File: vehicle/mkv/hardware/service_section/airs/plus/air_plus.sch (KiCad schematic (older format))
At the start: 11 parts, among them J1 UF_4_VT, J2 MicroFit_RA_06, J3 MicroFit_RA_4, J4 redcude_7461166, J5 redcude_7461166, K1 3350-4275-126(NC)

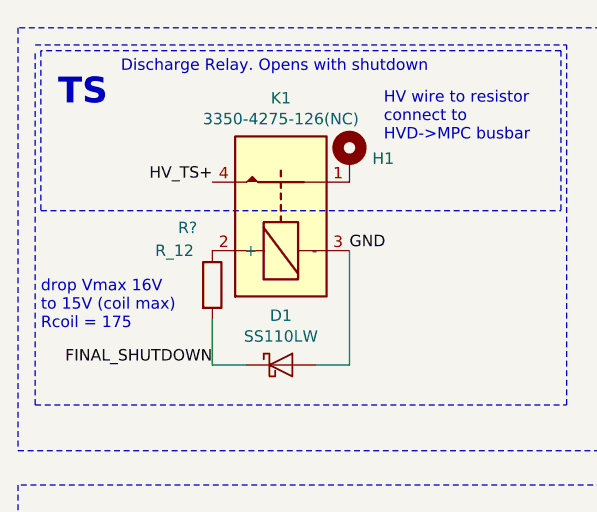
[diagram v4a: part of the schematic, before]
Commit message: fix: add resistor to limit relay voltage to operating range
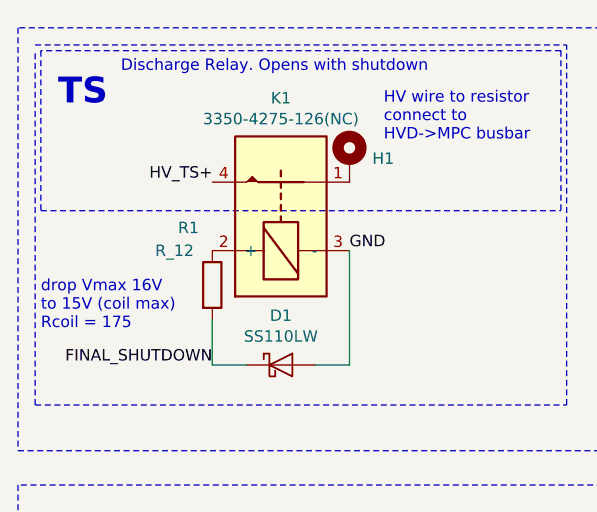
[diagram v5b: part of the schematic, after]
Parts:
- gave numbers to parts that had none: 1
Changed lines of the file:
@@
 drop Vmax 16V \nto 15V (coil max)\nRcoil = 175
 $Comp
-L formula:R_12 R?
+L formula:R_12 R1
 U 1 1 6262A6E0
 P 1600 1950
-F 0 "R?" H 1450 2200 50  0000 L CNN
+F 0 "R1" H 1450 2200 50  0000 L CNN
 F 1 "R_12" H 1350 2100 50  0000 L CNN
 F 2 "footprints:R_0805_OEM" V 1530 1950 50  0001 C CNN

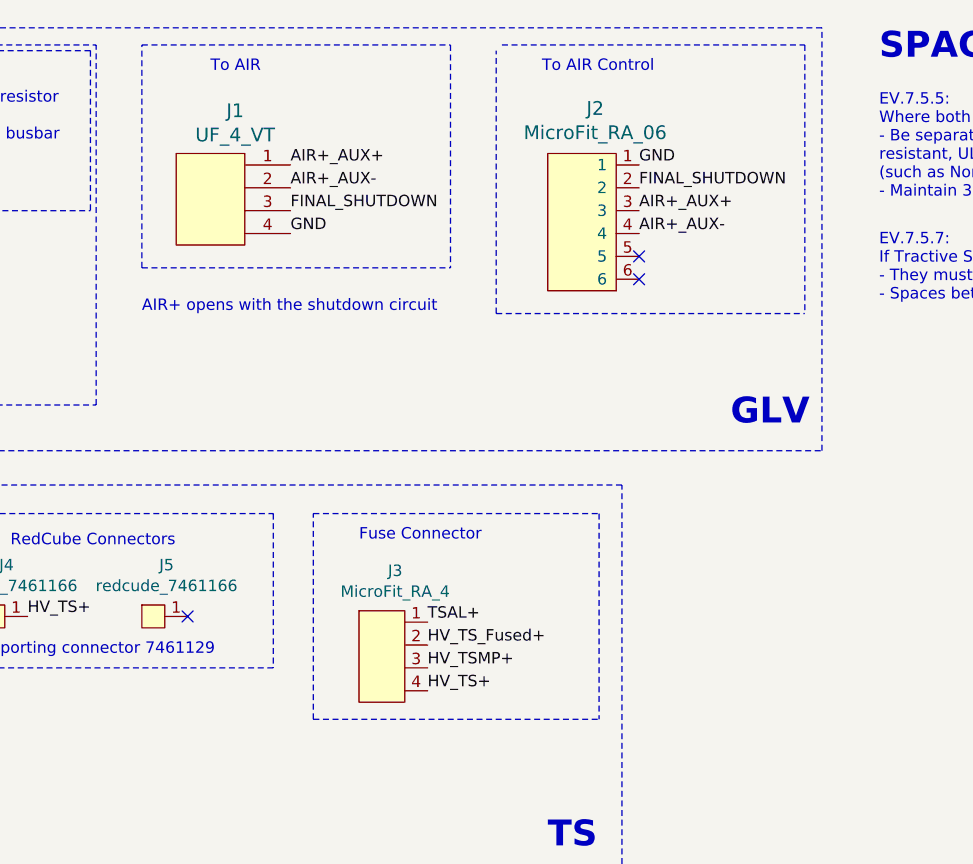
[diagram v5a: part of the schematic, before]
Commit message: feat: switch to microfit vt 4 where possible
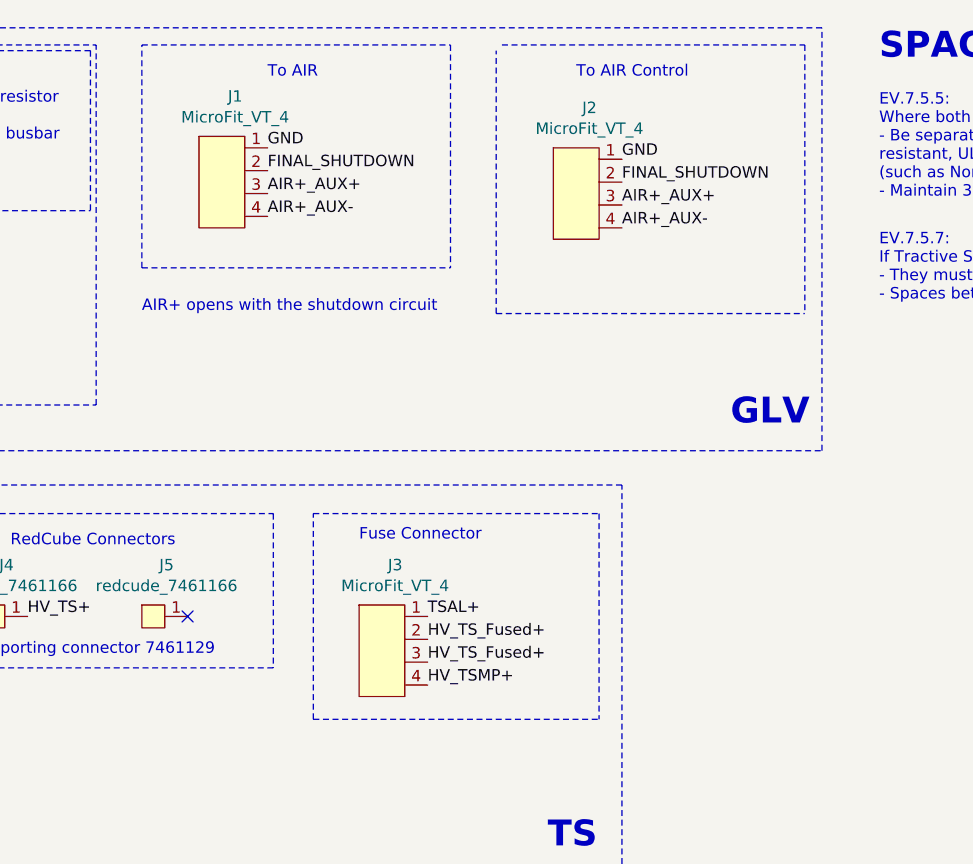
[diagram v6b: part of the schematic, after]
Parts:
- removed J1: UF_4_VT, footprints:Ultrafit_4, symbol Formula:UF_4_VT
- removed J2: MicroFit_RA_06, footprints:MicroFit_RA_06, symbol Formula:MicroFit_RA_06
- removed J3: MicroFit_RA_4, footprints:MicroFit_RA_4, symbol Formula:MicroFit_RA_4
- added J1, J2, J3: MicroFit_VT_4, footprints:MicroFit_VT_4, symbol formula:MicroFit_VT_4
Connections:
- net AIR+_AUX+: now also J1.3, J2.3
- net AIR+_AUX-: now also J1.4, J2.4
- net FINAL_SHUTDOWN: now also J1.2, J2.2
- net GND: now also J1.1, J2.1
- net HV_TSMP+: now also J3.4
- net HV_TS_Fused+: now also J3.1, J3.2, J3.3
- no-connect marks 3 -> 1
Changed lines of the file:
@@
 HV_TS+
-$Comp
-L Formula:UF_4_VT J1
-U 1 1 5DB02E97
-P 3650 1625
-F 0 "J1" H 3758 2062 60  0000 C CNN
-F 1 "UF_4_VT" H 3758 1956 60  0000 C CNN
-F 2 "footprints:Ultrafit_4" H 3550 1875 60  0001 C CNN
-F 3 "http://www.literature.molex.com/SQLImages/kelmscott/Molex/PDF_Images/987651-1008.pdf" H 3650 1975 60  0001 C CNN
-F 4 "DK" H 3650 1625 60  0001 C CNN "MFN"
-F 5 "WM11574-ND" H 3650 1625 60  0001 C CNN "MPN"
-F 6 "https://www.digikey.com/products/en?keywords=WM11574-ND" H 4150 2475 60  0001 C CNN "PurchasingLink"
-	1    3650 1625
-	1    0    0    -1
-$EndComp
 $Comp
 L Formula:redcude_7461166 J4
@@
 Text Label 1600 2300 2    50   ~ 0
 FINAL_SHUTDOWN
-Text Label 4000 1525 0    50   ~ 0
+Text Label 3900 1650 0    50   ~ 0
 AIR+_AUX-
-Text Label 4000 1425 0    50   ~ 0
+Text Label 3900 1550 0    50   ~ 0
 AIR+_AUX+
 Text Label 1625 3475 0    50   ~ 0
 HV_TSMP+
-Text Label 4000 1625 0    50   ~ 0
+Text Label 3900 1450 0    50   ~ 0
 FINAL_SHUTDOWN
-Text Label 4600 3725 0    50   ~ 0
-HV_TS+
-Text Label 4600 3625 0    50   ~ 0
+Text Label 4600 3700 0    50   ~ 0
 HV_TSMP+
-Text Label 4600 3425 0    50   ~ 0
+Text Label 4600 3400 0    50   ~ 0
 TSAL+
-$Comp
-L Formula:MicroFit_RA_4 J3
-U 1 1 5DF102AC
-P 4400 3575
-F 0 "J3" H 4458 3950 50  0000 C CNN
-F 1 "MicroFit_RA_4" H 4458 3859 50  0000 C CNN
-F 2 "footprints:MicroFit_RA_4" H 4400 3275 50  0001 C CNN
-F 3 "" H 4400 3575 100 0001 C CNN
-F 4 "https://www.digikey.com/product-detail/en/molex/0430450400/WM1814-ND/252527" H 4400 3575 50  0001 C CNN "Purchasing Link"
-	1    4400 3575
-	1    0    0    -1
-$EndComp
-Text Label 4600 3525 0    50   ~ 0
+Text Label 4600 3500 0    50   ~ 0
 HV_TS_Fused+
-NoConn ~ 5525 1925
-Text Label 5525 1525 0    50   ~ 0
+Text Label 5450 1500 0    50   ~ 0
 FINAL_SHUTDOWN
-Text Label 5525 1425 0    50   ~ 0
+Text Label 5450 1400 0    50   ~ 0
 GND
-Text Label 5525 1725 0    50   ~ 0
+Text Label 5450 1700 0    50   ~ 0
 AIR+_AUX-
-Text Label 5525 1625 0    50   ~ 0
+Text Label 5450 1600 0    50   ~ 0
 AIR+_AUX+
 Text Label 1950 4325 0    50   ~ 0
@@
 Text Notes 925  3100 0    50   ~ 0
 TSMP Body Protection Resistor
-Text Notes 3650 1025 0    50   ~ 0
+Text Notes 3900 1050 0    50   ~ 0
 To AIR\n
-Text Notes 5100 1025 0    50   ~ 0
+Text Notes 5250 1050 0    50   ~ 0
 To AIR Control\n
 Text Notes 4300 3075 0    50   ~ 0
@@
 Wire Notes Line
 	4900 2075 4900 925
-$Comp
-L Formula:MicroFit_RA_06 J2
-U 1 1 5DB019DF
-P 5275 1675
-F 0 "J2" H 5333 2172 60  0000 C CNN
-F 1 "MicroFit_RA_06" H 5333 2066 60  0000 C CNN
-F 2 "footprints:MicroFit_RA_06" H 5175 1925 60  0001 C CNN
-F 3 "https://www.molex.com/pdm_docs/sd/430450601_sd.pdf" H 5275 2025 60  0001 C CNN
-F 4 "Molex" H 5375 3075 60  0001 C CNN "MFN"
-F 5 "WM4037-ND" H 5475 3175 60  0001 C CNN "MPN"
-F 6 "https://www.digikey.com/product-detail/en/molex/0430450601/WM4037-ND/2421555" H 5275 2975 60  0001 C CNN "PurchasingLink"
-	1    5275 1675
-	1    0    0    -1
-$EndComp
 Wire Notes Line
 	3350 1875 3350 900
@@
 Text Notes 2350 1325 0    50   ~ 0
 HV wire to resistor\nconnect to \nHVD->MPC busbar
-Text Label 4000 1725 0    50   ~ 0
+Text Label 3900 1350 0    50   ~ 0
 GND
-NoConn ~ 5525 1825
 Text Label 1950 4125 0    50   ~ 0
 TSAL+
@@
 Wire Wire Line
 	1600 2100 1600 2300
+$Comp
+L formula:MicroFit_VT_4 J1
+U 1 1 626397F4
+P 3700 1500
+F 0 "J1" H 3758 1875 50  0000 C CNN
+F 1 "MicroFit_VT_4" H 3758 1784 50  0000 C CNN
+F 2 "footprints:MicroFit_VT_4" H 3700 1200 50  0001 C CNN
+F 3 "" H 3700 1450 50  0001 C CNN
+F 4 "430450414" H 3758 1783 50  0001 C CNN "MPN"
+F 5 "https://www.digikey.com/product-detail/en/molex/0430450414/WM1796-ND/252509" H 3758 1784 50  0001 C CNN "PurchasingLink"
+	1    3700 1500
+	1    0    0    -1
+$EndComp
+$Comp
+L formula:MicroFit_VT_4 J2
+U 1 1 62642CF5
+P 5250 1550
+F 0 "J2" H 5308 1925 50  0000 C CNN
+F 1 "MicroFit_VT_4" H 5308 1834 50  0000 C CNN
+F 2 "footprints:MicroFit_VT_4" H 5250 1250 50  0001 C CNN
+F 3 "" H 5250 1500 50  0001 C CNN
+F 4 "430450414" H 5308 1833 50  0001 C CNN "MPN"
+F 5 "https://www.digikey.com/product-detail/en/molex/0430450414/WM1796-ND/252509" H 5308 1834 50  0001 C CNN "PurchasingLink"
+	1    5250 1550
+	1    0    0    -1
+$EndComp
+$Comp
+L formula:MicroFit_VT_4 J3
+U 1 1 6264B27B
+P 4400 3550
+F 0 "J3" H 4458 3925 50  0000 C CNN
+F 1 "MicroFit_VT_4" H 4458 3834 50  0000 C CNN
+F 2 "footprints:MicroFit_VT_4" H 4400 3250 50  0001 C CNN
+F 3 "" H 4400 3500 50  0001 C CNN
+F 4 "430450414" H 4458 3833 50  0001 C CNN "MPN"
+F 5 "https://www.digikey.com/product-detail/en/molex/0430450414/WM1796-ND/252509" H 4458 3834 50  0001 C CNN "PurchasingLink"
+	1    4400 3550
+	1    0    0    -1
+$EndComp
+Text Label 4600 3600 0    50   ~ 0
+HV_TS_Fused+
 $EndSCHEMATC

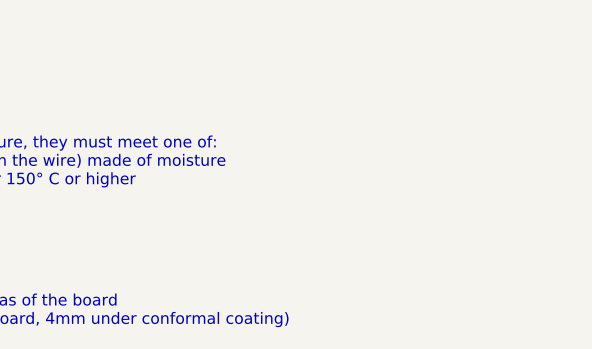
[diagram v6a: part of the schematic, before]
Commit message: fix: flip connector and remove extra labels
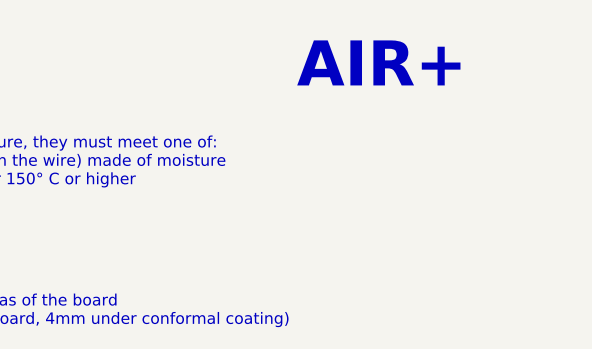
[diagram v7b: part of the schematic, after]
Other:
- note added: "AIR+"
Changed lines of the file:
@@
 Text Label 4600 3600 0    50   ~ 0
 HV_TS_Fused+
+Text Notes 10200 1000 0    197  ~ 39
+AIR+
 $EndSCHEMATC
